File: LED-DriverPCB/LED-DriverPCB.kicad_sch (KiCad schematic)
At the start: 44 parts, among them J1 Screw_Terminal_01x03, J12 Screw_Terminal_01x02, J13 Screw_Terminal_01x02, J14 Screw_Terminal_01x02, J15 Screw_Terminal_01x02, J16 Screw_Terminal_01x02, J17 Screw_Terminal_01x02, J18 Screw_Terminal_01x02, J19 Screw_Terminal_01x02, J2 Screw_Terminal_01x03, J20 Conn_ARM_SWD_TagConnect_TC2030, J3 Screw_Terminal_01x03, J4 Screw_Terminal_01x03, J5 Screw_Terminal_01x03, J6 Screw_Terminal_01x03, J7 Screw_Terminal_01x03, J8 Screw_Terminal_01x03, J9 USB_C_Receptacle_USB2.0_16P, SW1 SW_SPDT, U1 STM32F103RCTx, U2 TXB0108PW, U3 AMS1117-3.3, U4 USBLC6-2SC6, X1 8MHz

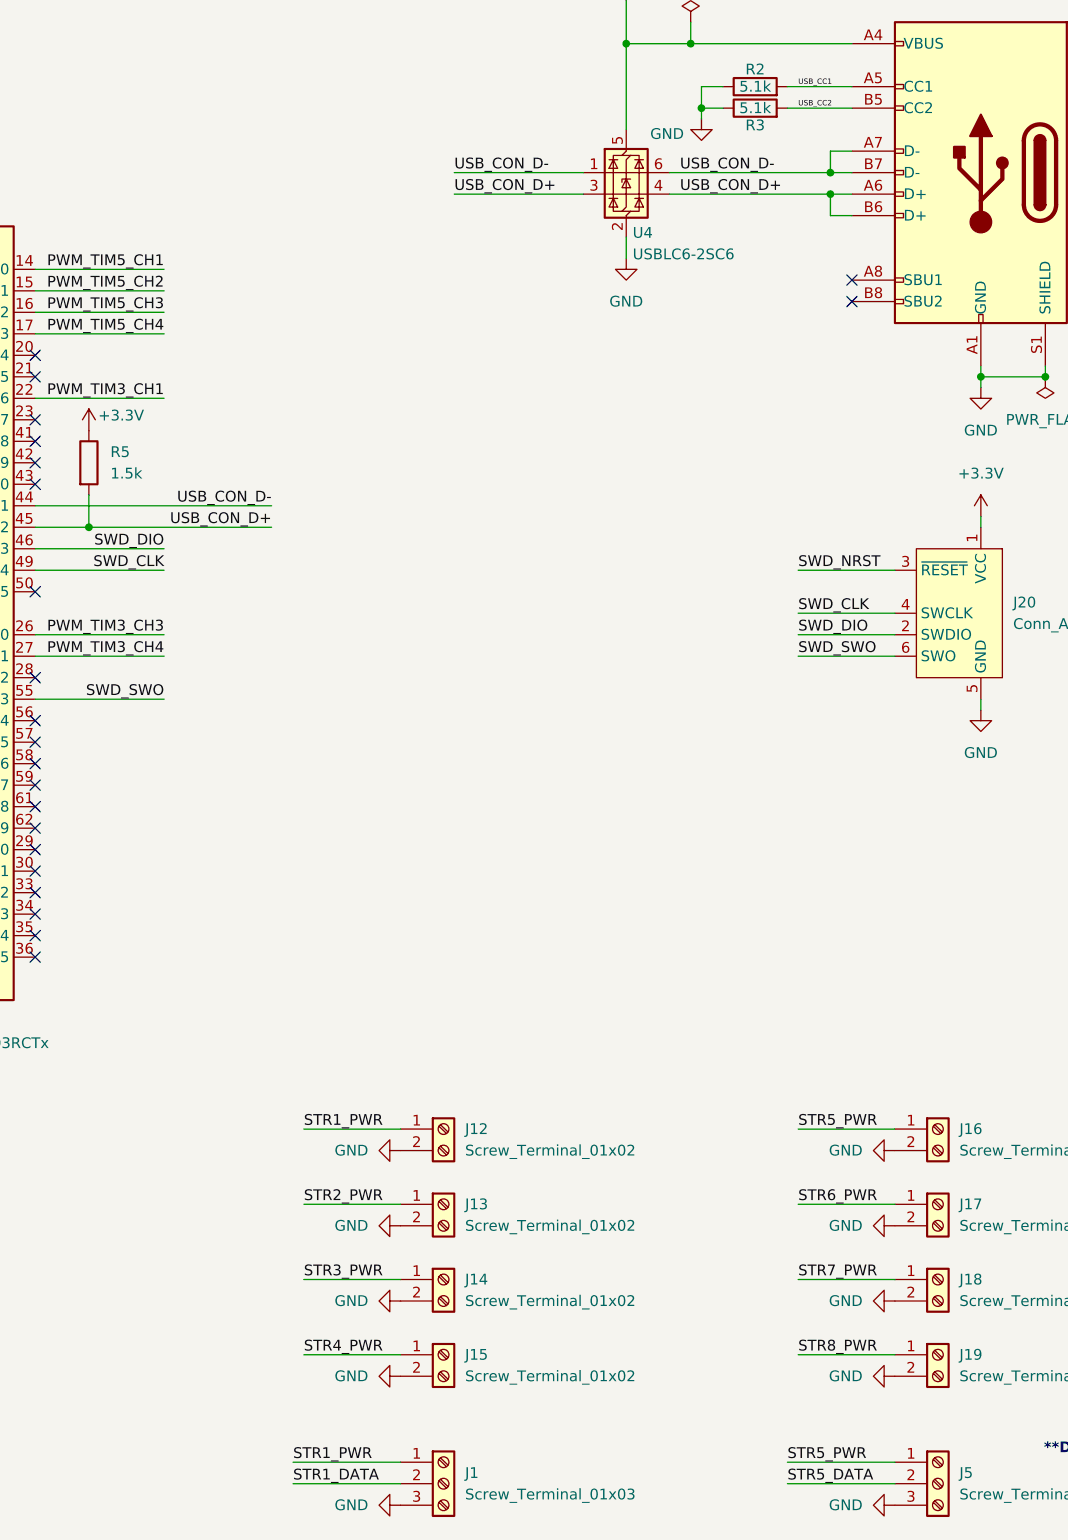
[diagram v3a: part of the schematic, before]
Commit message: Worked on PCB layout
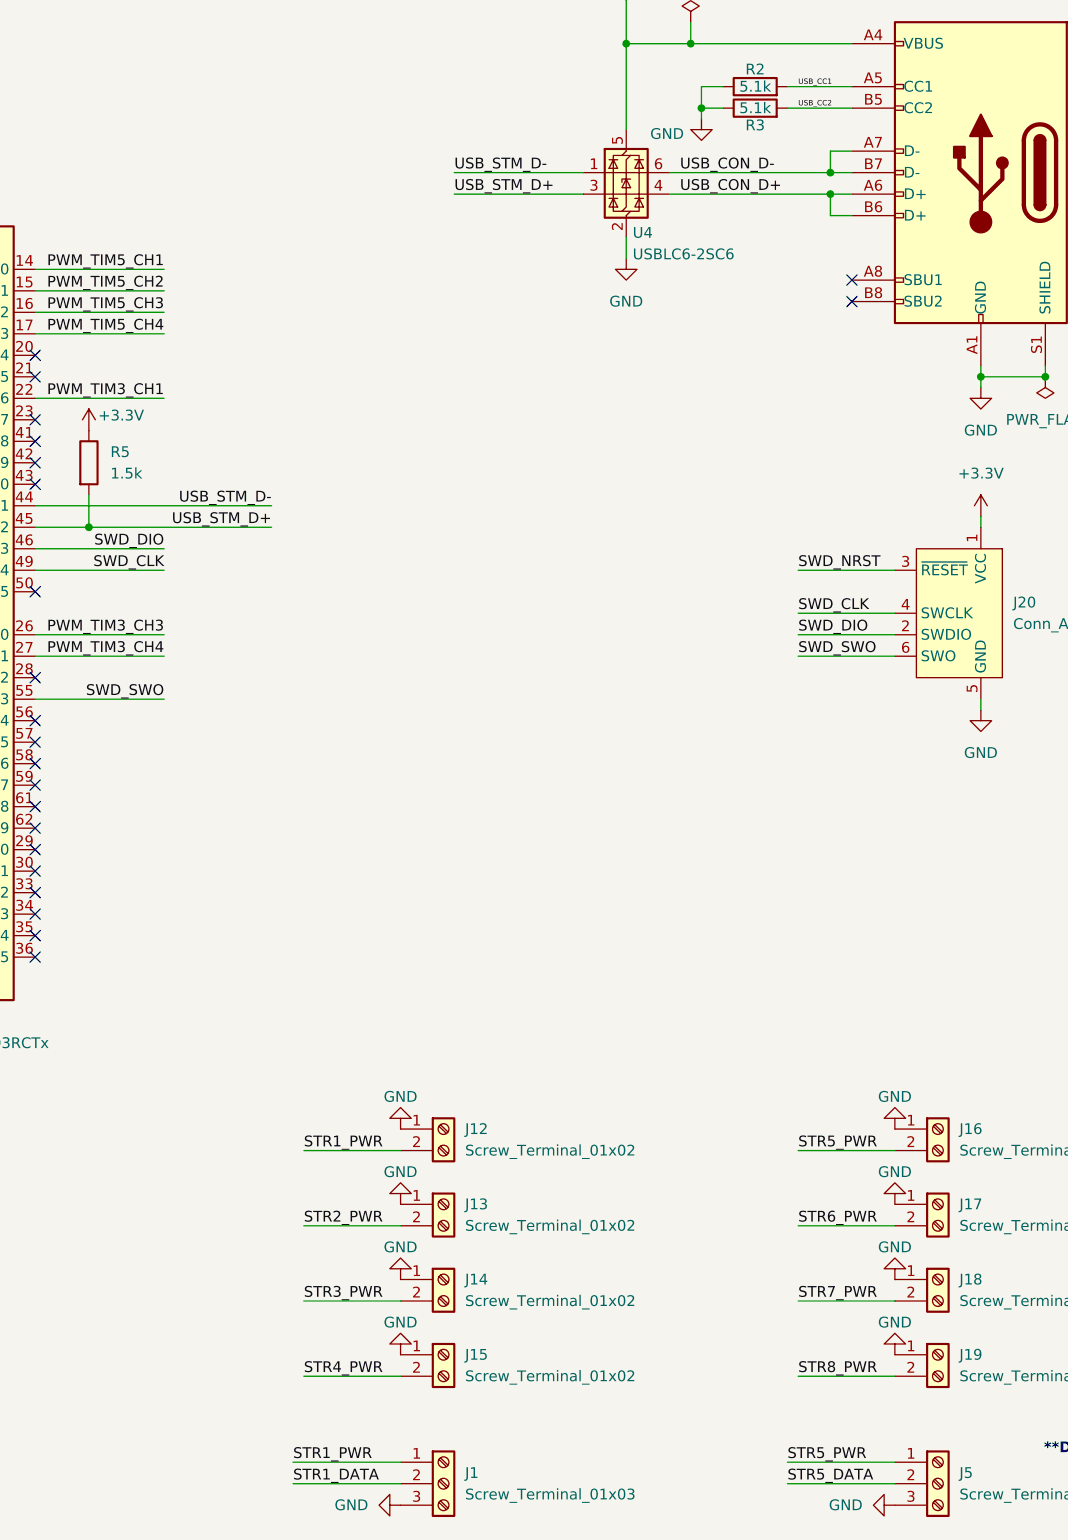
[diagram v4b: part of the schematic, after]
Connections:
- net GND: now also J12.1 (Pin_1), J13.1 (Pin_1), J14.1 (Pin_1), J15.1 (Pin_1), J16.1 (Pin_1), J17.1 (Pin_1), J18.1 (Pin_1), J19.1 (Pin_1); no longer J12.2 (Pin_2), J13.2 (Pin_2), J14.2 (Pin_2), J15.2 (Pin_2), J16.2 (Pin_2), J17.2 (Pin_2), J18.2 (Pin_2), J19.2 (Pin_2)
- net STR1_PWR: now also J12.2 (Pin_2); no longer J12.1 (Pin_1)
- net STR2_PWR: now also J13.2 (Pin_2); no longer J13.1 (Pin_1)
- net STR3_PWR: now also J14.2 (Pin_2); no longer J14.1 (Pin_1)
- net STR4_PWR: now also J15.2 (Pin_2); no longer J15.1 (Pin_1)
- net STR5_PWR: now also J16.2 (Pin_2); no longer J16.1 (Pin_1)
- net STR6_PWR: now also J17.2 (Pin_2); no longer J17.1 (Pin_1)
- net STR7_PWR: now also J18.2 (Pin_2); no longer J18.1 (Pin_1)
- net STR8_PWR: now also J19.2 (Pin_2); no longer J19.1 (Pin_1)
- net USB_CON_D+: no longer R5.2, U1.45 (PA12), U4.3 (I/O2)
- net USB_CON_D-: no longer U1.44 (PA11), U4.1 (I/O1)
- new net USB_STM_D+: R5.2, U1.45 (PA12), U4.3 (I/O2)
- new net USB_STM_D-: U1.44 (PA11), U4.1 (I/O1)

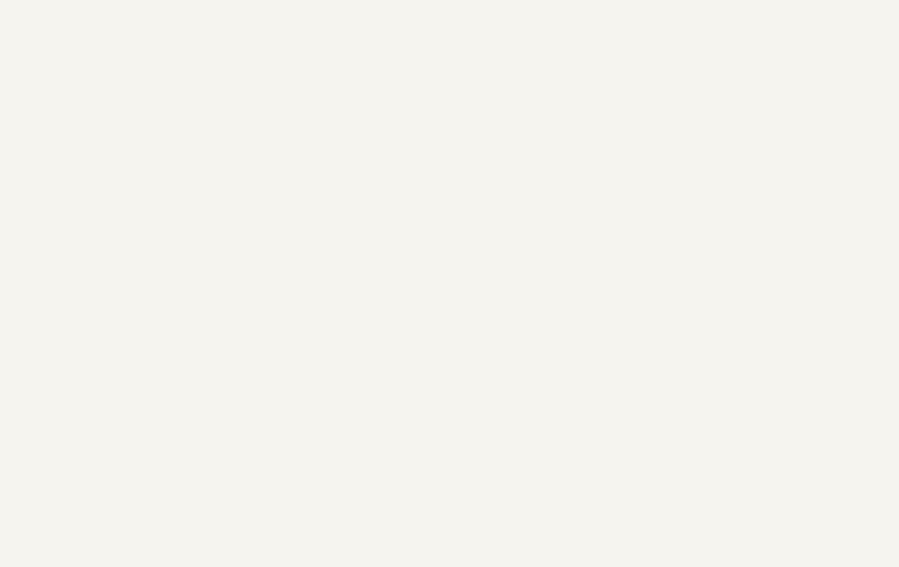
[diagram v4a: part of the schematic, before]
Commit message: Finished edge cuts
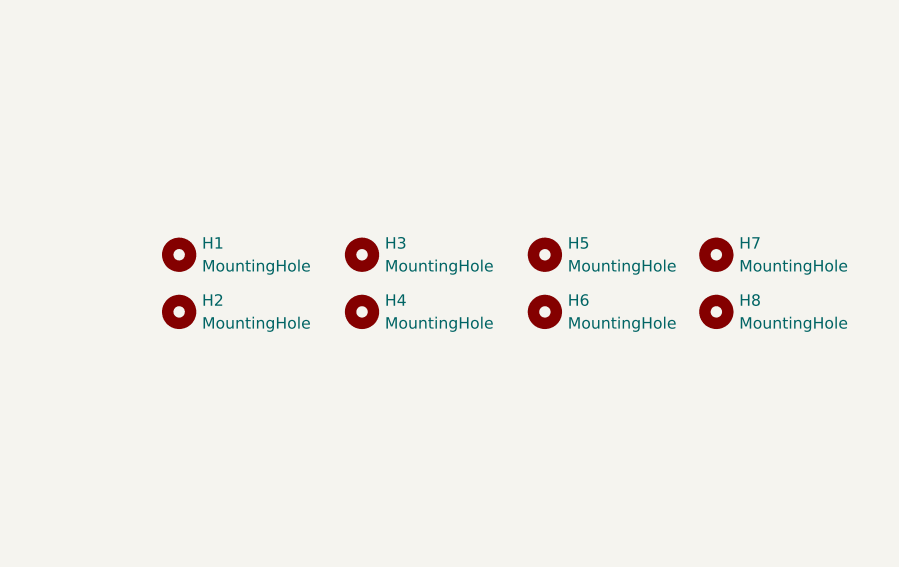
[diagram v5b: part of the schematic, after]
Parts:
- added H1, H2, H3, H4, H5, H6, H7, H8: MountingHole, MountingHole:MountingHole_3.2mm_M3, symbol Mechanical:MountingHole

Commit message: Placed parts
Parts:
- removed SW1: SW_SPDT, Button_Switch_SMD:SW_SPDT_PCM12, symbol Switch:SW_SPDT
- H1, H2, H3, H4, H5, H6, H7, H8: footprint MountingHole:MountingHole_3.2mm_M3 -> (none)
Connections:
- net SW_BOOT is gone; now on net GND: R1.1
- net SHIFTER_OE: now reaches R4.2, U2.10 (OE)
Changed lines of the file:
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@@
 	(wire
 		(pts
-			(xy 60.96 74.93) (xy 69.85 74.93)
-		)
-		(stroke
-			(width 0)
-			(type default)
-		)
-	)
-	(wire
-		(pts
 			(xy 64.77 99.06) (xy 57.15 99.06)
 		)
@@
 	(wire
 		(pts
-			(xy 46.99 71.12) (xy 46.99 72.39)
-		)
-		(stroke
-			(width 0)
-			(type default)
-		)
-	)
-	(wire
-		(pts
 			(xy 21.59 45.72) (xy 33.02 45.72)
 		)
@@
 	(wire
 		(pts
-			(xy 46.99 77.47) (xy 50.8 77.47)
+			(xy 64.77 74.93) (xy 69.85 74.93)
 		)
 		(stroke
@@
 	(wire
 		(pts
-			(xy 46.99 78.74) (xy 46.99 77.47)
+			(xy 64.77 76.2) (xy 64.77 74.93)
 		)
 		(stroke
@@
 	(wire
 		(pts
-			(xy 46.99 72.39) (xy 50.8 72.39)
-		)
-		(stroke
-			(width 0)
-			(type default)
-		)
-	)
-	(wire
-		(pts
 			(xy 191.77 43.18) (xy 191.77 53.34)
 		)
@@
 		)
 	)
-	(label "SW_BOOT"
-		(at 63.5 74.93 0)
-		(effects
-			(font
-				(size 0.635 0.635)
-			)
-			(justify left bottom)
-		)
-	)
 	(label "STR2_DATA"
 		(at 80.01 245.11 180)
@@
 		)
 	)
+	(label "SHIFTER_OE"
+		(at 31.75 240.03 0)
+		(effects
+			(font
+				(size 1.27 1.27)
+			)
+			(justify left bottom)
+		)
+	)
 	(label "PWM_TIM3_CH4"
 		(at 137.16 115.57 180)
@@
 	)
 	(symbol
-		(lib_id "Switch:SW_SPDT")
-		(at 55.88 74.93 180)
-		(unit 1)
-		(exclude_from_sim no)
-		(in_bom yes)
-		(on_board yes)
-		(dnp no)
-		(fields_autoplaced yes)
-		(property "Reference" "SW1"
-			(at 55.88 66.04 0)
-			(effects
-				(font
-					(size 1.27 1.27)
-				)
-			)
-		)
-		(property "Value" "SW_SPDT"
-			(at 55.88 68.58 0)
-			(effects
-				(font
-					(size 1.27 1.27)
-				)
-			)
-		)
-		(property "Footprint" "Button_Switch_SMD:SW_SPDT_PCM12"
-			(at 55.88 74.93 0)
-			(effects
-				(font
-					(size 1.27 1.27)
-				)
-				(hide yes)
-			)
-		)
-		(property "Datasheet" "~"
-			(at 55.88 67.31 0)
-			(effects
-				(font
-					(size 1.27 1.27)
-				)
-				(hide yes)
-			)
-		)
-		(property "Description" "Switch, single pole double throw"
-			(at 55.88 74.93 0)
-			(effects
-				(font
-					(size 1.27 1.27)
-				)
-				(hide yes)
-			)
-		)
-		(pin "1"
-		)
-		(pin "3"
-		)
-		(pin "2"
-		)
-		(instances
-			(project ""
-				(path "/f8915909-606a-4747-b712-208c2aaca226"
-					(reference "SW1")
-					(unit 1)
-				)
-			)
-		)
-	)
-	(symbol
 		(lib_id "Device:C")
 		(at 55.88 53.34 0)
@@
 			)
 		)
-		(property "Footprint" "MountingHole:MountingHole_3.2mm_M3"
+		(property "Footprint" ""
 			(at 294.64 50.8 0)
 			(effects
@@
 			)
 		)
-		(property "Footprint" "MountingHole:MountingHole_3.2mm_M3"
+		(property "Footprint" ""
 			(at 354.33 50.8 0)
 			(effects
@@
 			)
 		)
-		(property "Footprint" "MountingHole:MountingHole_3.2mm_M3"
+		(property "Footprint" ""
 			(at 294.64 44.45 0)
 			(effects
@@
 			)
 		)
-		(property "Footprint" "MountingHole:MountingHole_3.2mm_M3"
+		(property "Footprint" ""
 			(at 314.96 50.8 0)
 			(effects
@@
 	(symbol
 		(lib_id "power:GND")
-		(at 46.99 78.74 0)
+		(at 64.77 76.2 0)
 		(unit 1)
 		(exclude_from_sim no)
@@
 		(dnp no)
 		(property "Reference" "#PWR01"
-			(at 46.99 85.09 0)
+			(at 64.77 82.55 0)
 			(effects
 				(font
@@
 		)
 		(property "Value" "GND"
-			(at 42.926 80.264 0)
+			(at 60.706 77.724 0)
 			(effects
 				(font
@@
 		)
 		(property "Footprint" ""
-			(at 46.99 78.74 0)
+			(at 64.77 76.2 0)
 			(effects
 				(font
@@
 		)
 		(property "Datasheet" ""
-			(at 46.99 78.74 0)
+			(at 64.77 76.2 0)
 			(effects
 				(font
@@
 		)
 		(property "Description" "Power symbol creates a global label with name \"GND\" , ground"
-			(at 46.99 78.74 0)
+			(at 64.77 76.2 0)
 			(effects
 				(font
@@
 			)
 		)
-		(property "Footprint" "MountingHole:MountingHole_3.2mm_M3"
+		(property "Footprint" ""
 			(at 335.28 44.45 0)
 			(effects
@@
 			)
 		)
-		(property "Footprint" "MountingHole:MountingHole_3.2mm_M3"
+		(property "Footprint" ""
 			(at 354.33 44.45 0)
 			(effects
@@
 	(symbol
 		(lib_id "power:+3.3V")
-		(at 46.99 71.12 0)
-		(unit 1)
-		(exclude_from_sim no)
-		(in_bom yes)
-		(on_board yes)
-		(dnp no)
-		(fields_autoplaced yes)
-		(property "Reference" "#PWR03"
-			(at 46.99 74.93 0)
-			(effects
-				(font
-					(size 1.27 1.27)
-				)
-				(hide yes)
-			)
-		)
-		(property "Value" "+3.3V"
-			(at 46.99 66.04 0)
-			(effects
-				(font
-					(size 1.27 1.27)
-				)
-			)
-		)
-		(property "Footprint" ""
-			(at 46.99 71.12 0)
-			(effects
-				(font
-					(size 1.27 1.27)
-				)
-				(hide yes)
-			)
-		)
-		(property "Datasheet" ""
-			(at 46.99 71.12 0)
-			(effects
-				(font
-					(size 1.27 1.27)
-				)
-				(hide yes)
-			)
-		)
-		(property "Description" "Power symbol creates a global label with name \"+3.3V\""
-			(at 46.99 71.12 0)
-			(effects
-				(font
-					(size 1.27 1.27)
-				)
-				(hide yes)
-			)
-		)
-		(pin "1"
-		)
-		(instances
-			(project ""
-				(path "/f8915909-606a-4747-b712-208c2aaca226"
-					(reference "#PWR03")
-					(unit 1)
-				)
-			)
-		)
-	)
-	(symbol
-		(lib_id "power:+3.3V")
 		(at 233.68 99.06 0)
 		(unit 1)
@@
 			)
 		)
-		(property "Footprint" "MountingHole:MountingHole_3.2mm_M3"
+		(property "Footprint" ""
 			(at 314.96 44.45 0)
 			(effects
@@
 			)
 		)
-		(property "Footprint" "MountingHole:MountingHole_3.2mm_M3"
+		(property "Footprint" ""
 			(at 335.28 50.8 0)
 			(effects
@@
 		(on_board yes)
 		(dnp no)
-		(fields_autoplaced yes)
 		(property "Reference" "#PWR019"
 			(at 40.64 238.76 0)
@@
 		)
 		(property "Value" "GND"
-			(at 40.64 237.49 0)
+			(at 44.196 234.442 0)
 			(effects
 				(font

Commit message: Started routing
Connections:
- net USB_CON_D+: now also U4.6 (I/O1); no longer U4.4 (I/O2)
- net USB_CON_D-: now also U4.4 (I/O2); no longer U4.6 (I/O1)
- net USB_STM_D+: now also U4.1 (I/O1); no longer U4.3 (I/O2)
- net USB_STM_D-: now also U4.3 (I/O2); no longer U4.1 (I/O1)
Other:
- moved on the sheet: U4
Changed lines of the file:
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@@
 	)
 	(junction
-		(at 191.77 43.18)
-		(diameter 0)
-		(color 0 0 0 0)
-	)
-	(junction
 		(at 78.74 59.69)
 		(diameter 0)
@@
 	)
 	(junction
+		(at 189.23 43.18)
+		(diameter 0)
+		(color 0 0 0 0)
+	)
+	(junction
 		(at 215.9 60.96)
 		(diameter 0)
@@
 	(wire
 		(pts
-			(xy 191.77 43.18) (xy 199.39 43.18)
-		)
-		(stroke
-			(width 0)
-			(type default)
-		)
-	)
-	(wire
-		(pts
 			(xy 66.04 247.65) (xy 80.01 247.65)
 		)
@@
 	(wire
 		(pts
+			(xy 189.23 77.47) (xy 189.23 78.74)
+		)
+		(stroke
+			(width 0)
+			(type default)
+		)
+	)
+	(wire
+		(pts
 			(xy 78.74 45.72) (xy 90.17 45.72)
 		)
@@
 	(wire
 		(pts
-			(xy 171.45 58.42) (xy 186.69 58.42)
+			(xy 168.91 72.39) (xy 184.15 72.39)
 		)
 		(stroke
@@
 	(wire
 		(pts
-			(xy 191.77 66.04) (xy 191.77 68.58)
-		)
-		(stroke
-			(width 0)
-			(type default)
-		)
-	)
-	(wire
-		(pts
 			(xy 210.82 210.82) (xy 223.52 210.82)
 		)
@@
 	(wire
 		(pts
-			(xy 191.77 38.1) (xy 191.77 43.18)
+			(xy 189.23 38.1) (xy 189.23 43.18)
 		)
 		(stroke
@@
 	(wire
 		(pts
-			(xy 171.45 60.96) (xy 186.69 60.96)
+			(xy 168.91 69.85) (xy 184.15 69.85)
 		)
 		(stroke
@@
 	(wire
 		(pts
+			(xy 189.23 43.18) (xy 189.23 64.77)
+		)
+		(stroke
+			(width 0)
+			(type default)
+		)
+	)
+	(wire
+		(pts
 			(xy 66.04 252.73) (xy 80.01 252.73)
 		)
@@
 	(wire
 		(pts
+			(xy 189.23 43.18) (xy 199.39 43.18)
+		)
+		(stroke
+			(width 0)
+			(type default)
+		)
+	)
+	(wire
+		(pts
 			(xy 90.17 45.72) (xy 90.17 49.53)
 		)
@@
 	(wire
 		(pts
+			(xy 194.31 72.39) (xy 212.09 72.39)
+		)
+		(stroke
+			(width 0)
+			(type default)
+		)
+	)
+	(wire
+		(pts
 			(xy 111.76 60.96) (xy 111.76 62.23)
 		)
@@
 	(wire
 		(pts
-			(xy 191.77 43.18) (xy 191.77 53.34)
-		)
-		(stroke
-			(width 0)
-			(type default)
-		)
-	)
-	(wire
-		(pts
 			(xy 67.31 59.69) (xy 78.74 59.69)
 		)
@@
 	(wire
 		(pts
+			(xy 194.31 69.85) (xy 212.09 69.85)
+		)
+		(stroke
+			(width 0)
+			(type default)
+		)
+	)
+	(wire
+		(pts
 			(xy 212.09 115.57) (xy 223.52 115.57)
 		)
@@
 		)
 	)
+	(label "USB_CON_D-"
+		(at 212.09 72.39 180)
+		(effects
+			(font
+				(size 1.27 1.27)
+			)
+			(justify right bottom)
+		)
+	)
 	(label "PWM_TIM5_CH2"
 		(at 29.21 245.11 0)
@@
 		)
 	)
+	(label "USB_CON_D+"
+		(at 212.09 69.85 180)
+		(effects
+			(font
+				(size 1.27 1.27)
+			)
+			(justify right bottom)
+		)
+	)
 	(label "USB_STM_D-"
 		(at 149.86 97.79 180)
@@
 	)
 	(label "USB_STM_D-"
-		(at 171.45 58.42 0)
+		(at 168.91 72.39 0)
 		(effects
 			(font
@@
 	)
 	(label "USB_STM_D+"
-		(at 171.45 60.96 0)
+		(at 168.91 69.85 0)
 		(effects
 			(font
@@
 	(symbol
 		(lib_id "power:GND")
-		(at 191.77 68.58 0)
-		(unit 1)
-		(exclude_from_sim no)
-		(in_bom yes)
-		(on_board yes)
-		(dnp no)
-		(fields_autoplaced yes)
-		(property "Reference" "#PWR09"
-			(at 191.77 74.93 0)
-			(effects
-				(font
-					(size 1.27 1.27)
-				)
-				(hide yes)
-			)
-		)
-		(property "Value" "GND"
-			(at 191.77 73.66 0)
-			(effects
-				(font
-					(size 1.27 1.27)
-				)
-			)
-		)
-		(property "Footprint" ""
-			(at 191.77 68.58 0)
-			(effects
-				(font
-					(size 1.27 1.27)
-				)
-				(hide yes)
-			)
-		)
-		(property "Datasheet" ""
-			(at 191.77 68.58 0)
-			(effects
-				(font
-					(size 1.27 1.27)
-				)
-				(hide yes)
-			)
-		)
-		(property "Description" "Power symbol creates a global label with name \"GND\" , ground"
-			(at 191.77 68.58 0)
-			(effects
-				(font
-					(size 1.27 1.27)
-				)
-				(hide yes)
-			)
-		)
-		(pin "1"
-		)
-		(instances
-			(project "LED-DriverPCB"
-				(path "/f8915909-606a-4747-b712-208c2aaca226"
-					(reference "#PWR09")
-					(unit 1)
-				)
-			)
-		)
-	)
-	(symbol
-		(lib_id "power:GND")
 		(at 21.59 60.96 0)
 		(unit 1)
@@
 	(symbol
 		(lib_id "Power_Protection:USBLC6-2SC6")
-		(at 191.77 58.42 0)
+		(at 189.23 69.85 0)
 		(unit 1)
 		(exclude_from_sim no)
@@
 		(dnp no)
 		(property "Reference" "U4"
-			(at 192.532 65.532 0)
+			(at 189.992 76.962 0)
 			(effects
 				(font
@@
 		)
 		(property "Value" "USBLC6-2SC6"
-			(at 192.532 68.072 0)
+			(at 189.992 79.502 0)
 			(effects
 				(font
@@
 		)
 		(property "Footprint" "Package_TO_SOT_SMD:SOT-23-6"
-			(at 193.04 64.77 0)
+			(at 190.5 76.2 0)
 			(effects
 				(font
@@
 		)
 		(property "Datasheet" "https://www.st.com/resource/en/datasheet/usblc6-2.pdf"
-			(at 193.04 66.675 0)
+			(at 190.5 78.105 0)
 			(effects
 				(font
@@
 		)
 		(property "Description" "Very low capacitance ESD protection diode, 2 data-line, SOT-23-6"
-			(at 191.77 58.42 0)
+			(at 189.23 69.85 0)
 			(effects
 				(font
@@
 	)
 	(symbol
+		(lib_id "power:GND")
+		(at 189.23 78.74 0)
+		(unit 1)
+		(exclude_from_sim no)
+		(in_bom yes)
+		(on_board yes)
+		(dnp no)
+		(fields_autoplaced yes)
+		(property "Reference" "#PWR03"
+			(at 189.23 85.09 0)
+			(effects
+				(font
+					(size 1.27 1.27)
+				)
+				(hide yes)
+			)
+		)
+		(property "Value" "GND"
+			(at 189.23 83.82 0)
+			(effects
+				(font
+					(size 1.27 1.27)
+				)
+			)
+		)
+		(property "Footprint" ""
+			(at 189.23 78.74 0)
+			(effects
+				(font
+					(size 1.27 1.27)
+				)
+				(hide yes)
+			)
+		)
+		(property "Datasheet" ""
+			(at 189.23 78.74 0)
+			(effects
+				(font
+					(size 1.27 1.27)
+				)
+				(hide yes)
+			)
+		)
+		(property "Description" "Power symbol creates a global label with name \"GND\" , ground"
+			(at 189.23 78.74 0)
+			(effects
+				(font
+					(size 1.27 1.27)
+				)
+				(hide yes)
+			)
+		)
+		(pin "1"
+		)
+		(instances
+			(project ""
+				(path "/f8915909-606a-4747-b712-208c2aaca226"
+					(reference "#PWR03")
+					(unit 1)
+				)
+			)
+		)
+	)
+	(symbol
 		(lib_id "Connector:Screw_Terminal_01x03")
 		(at 228.6 213.36 0)
@@
 	(symbol
 		(lib_id "power:VBUS")
-		(at 191.77 38.1 0)
+		(at 189.23 38.1 0)
 		(unit 1)
 		(exclude_from_sim no)
@@
 		(fields_autoplaced yes)
 		(property "Reference" "#PWR08"
-			(at 191.77 41.91 0)
+			(at 189.23 41.91 0)
 			(effects
 				(font
@@
 		)
 		(property "Value" "VBUS"
-			(at 191.77 33.02 0)
+			(at 189.23 33.02 0)
 			(effects
 				(font
@@
 		)
 		(property "Footprint" ""
-			(at 191.77 38.1 0)
+			(at 189.23 38.1 0)
 			(effects
 				(font
@@
 		)
 		(property "Datasheet" ""
-			(at 191.77 38.1 0)
+			(at 189.23 38.1 0)
 			(effects
 				(font
@@
 		)
 		(property "Description" "Power symbol creates a global label with name \"VBUS\""
-			(at 191.77 38.1 0)
+			(at 189.23 38.1 0)
 			(effects
 				(font
